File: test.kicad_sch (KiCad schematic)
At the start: 19 parts, among them J1 Conn_01x04_Male, J2 Screw_Terminal_01x03, Q1 2N7000, Q2 2N7000, Q3 2N3904, Q4 2N3906, Q5 2N3904, Q6 2N3906, Q7 STP20NF06, Q8 STP20NF06

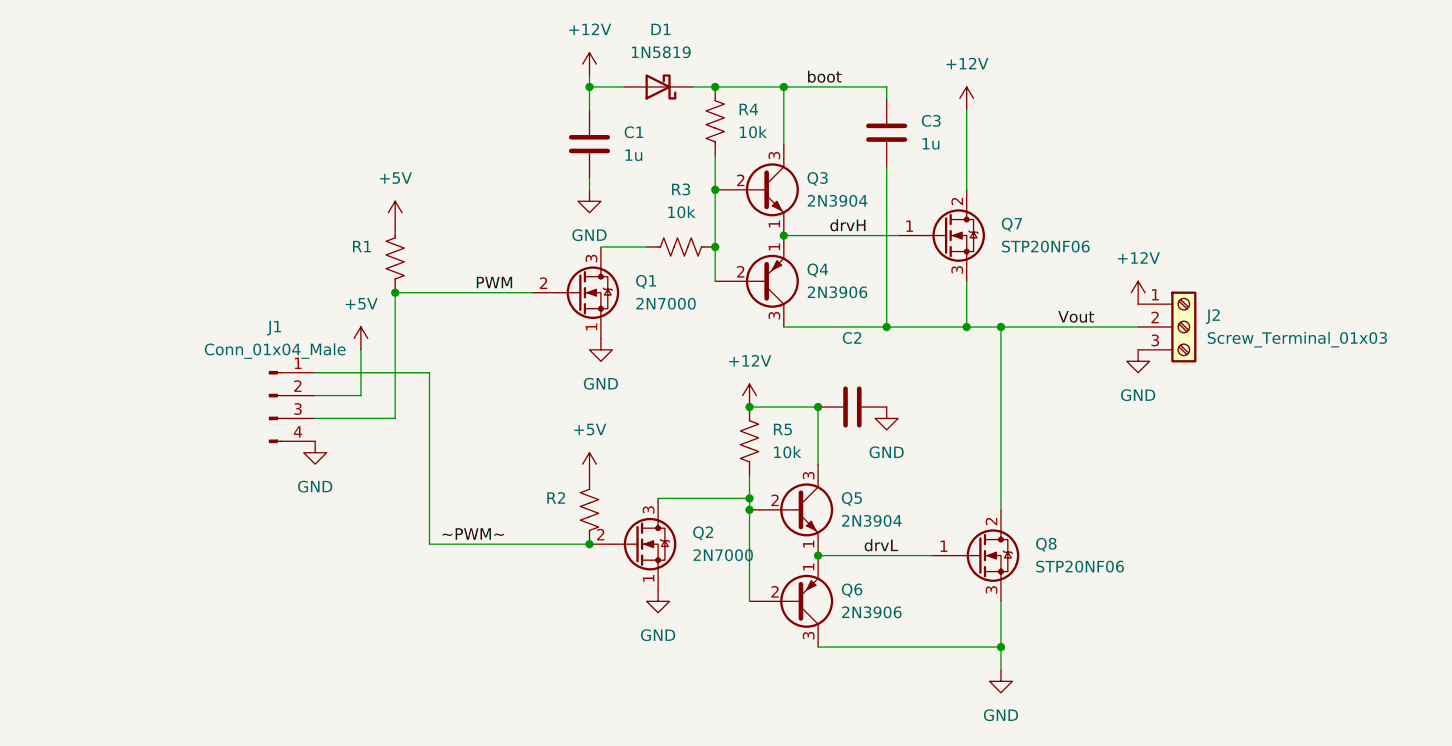
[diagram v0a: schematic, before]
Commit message: Reduced the unique parts count by consolidating resistors and capacitors
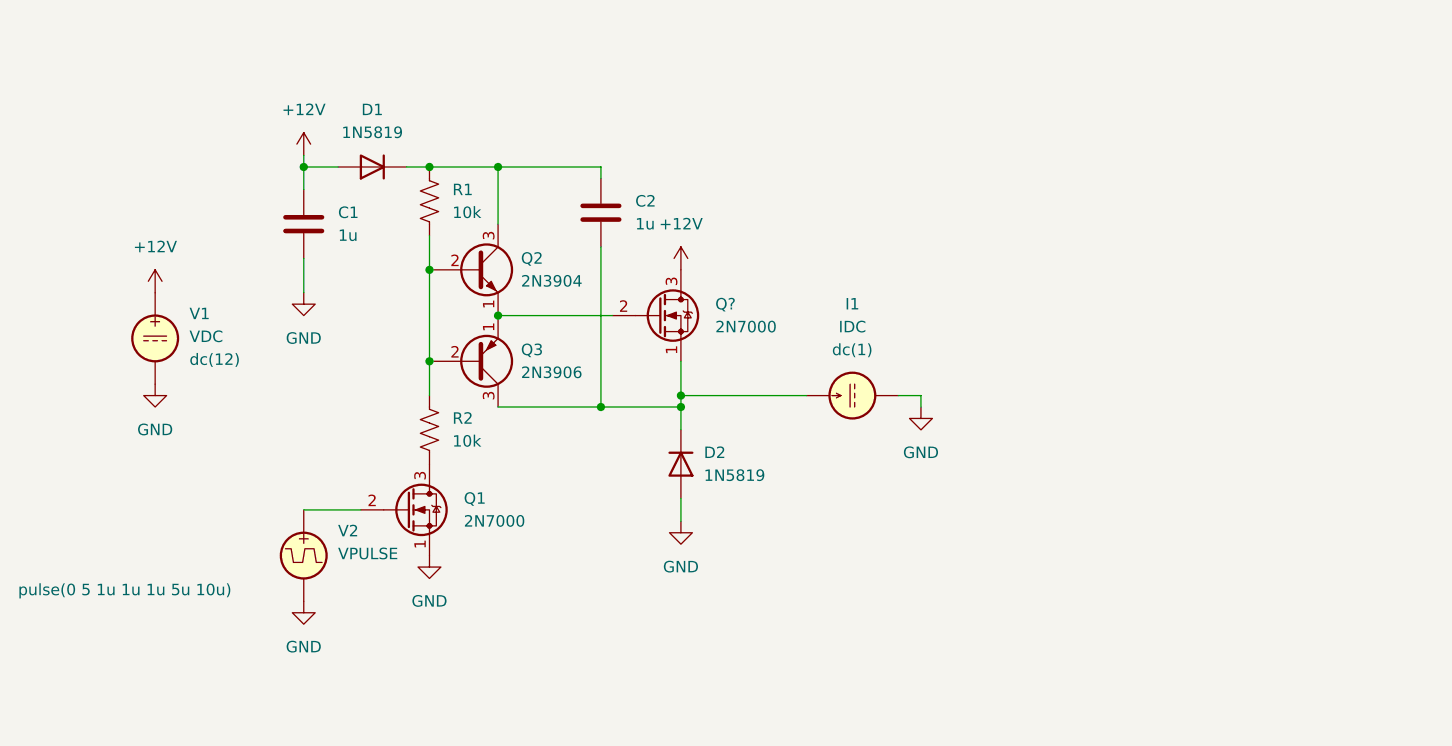
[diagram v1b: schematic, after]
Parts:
- removed C2: (no value), Capacitor_THT:C_Disc_D3.0mm_W1.6mm_P2.50mm, symbol Device:C
- removed D1: 1N5819, Diode_THT:D_DO-41_SOD81_P5.08mm_Vertical_AnodeUp, symbol Diode:1N5819
- removed J1: Conn_01x04_Male, Connector_PinHeader_2.54mm:PinHeader_1x04_P2.54mm_Vertical, symbol Connector:Conn_01x04_Male
- removed J2: Screw_Terminal_01x03, Connector_Phoenix_MC:PhoenixContact_MCV_1,5_3-G-3.5_1x03_P3.50mm_Vertical, symbol Connector:Screw_Terminal_01x03
- removed Q1: 2N7000, Package_TO_SOT_THT:TO-92_Inline, symbol Transistor_FET:2N7000
- removed Q3: 2N3904, Package_TO_SOT_THT:TO-92_Inline, symbol Transistor_BJT:2N3904
- removed Q4: 2N3906, Package_TO_SOT_THT:TO-92_Inline, symbol Transistor_BJT:2N3906
- removed Q7, Q8: STP20NF06, Package_TO_SOT_THT:TO-220-3_Vertical, symbol Device:Q_NMOS_GDS
- removed R1, R2: (no value), Resistor_THT:R_Axial_DIN0204_L3.6mm_D1.6mm_P2.54mm_Vertical, symbol Device:R_US
- removed R5: 10k, Resistor_THT:R_Axial_DIN0204_L3.6mm_D1.6mm_P2.54mm_Vertical, symbol Device:R_US
- added D1, D2: 1N5819, symbol Device:D
- added I1: IDC, symbol Simulation_SPICE:IDC
- added Q?: 2N7000, Package_TO_SOT_THT:TO-92_Inline, symbol Transistor_FET:2N7000
- added V1: VDC, symbol Simulation_SPICE:VDC
- added V2: VPULSE, symbol Simulation_SPICE:VPULSE
- C1: footprint Capacitor_THT:C_Disc_D3.0mm_W1.6mm_P2.50mm -> (none)
- C2: renamed from C3; footprint Capacitor_THT:C_Disc_D3.0mm_W1.6mm_P2.50mm -> (none)
- R1: renamed from R4; footprint Resistor_THT:R_Axial_DIN0204_L3.6mm_D1.6mm_P2.54mm_Vertical -> (none)
- R2: renamed from R3; footprint Resistor_THT:R_Axial_DIN0204_L3.6mm_D1.6mm_P2.54mm_Vertical -> (none)
- renumbered Q2 to Q1, Q5 to Q2, Q6 to Q3
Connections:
- net +12V: now also D1.2 (A), Q?.3 (D), V1.1; no longer Q2.3 (C)
- net GND: now also D2.2 (A), I1.2, V1.2, V2.2; no longer Q3.3 (C)
- net at Q2.2 (B), Q3.2 (B): now also R1.2, R2.1; no longer Q1.3 (D)
- net at R2.2: now also Q1.3 (D); no longer R1.2
- net Vout: no longer names the net of C2.2
- net Vout: now also Q3.3 (C), D2.1 (K), I1.1, Q?.1 (S)
- net boot: no longer names the net of C2.1, R1.1
- net boot: now also Q2.3 (C), D1.1 (K)
- net drvL: no longer names the net of Q2.1 (E), Q3.1 (E)
- net drvL: now also Q?.2 (G)
- net ~PWM~: no longer names the net of Q1.2 (G)
- net ~PWM~: now also V2.1
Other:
- moved on the sheet: C1, C2, Q1, Q2, Q3, R1, R2
